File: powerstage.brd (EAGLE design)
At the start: 41.9 x 43.5 mm, 44 parts, among them CON1 PINHEAD_1X10-2-FEMALE, CON2 PINHEAD_1X10-2-FEMALE, CON3 BATTERY_CON-2P-XT30-RA, IC1 MCP9700, Q1 BUK9K6R2-40E,115, Q2 BUK9K6R2-40E,115, Q3 BUK9K6R2-40E,115

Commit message: Bloody fiducial marks
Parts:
- moved U$9 38.6 mm to (11.3, 16.6), flipped to the bottom
- moved U$8 9.24 mm to (-16.6, -11.3), flipped to the bottom
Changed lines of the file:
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@@
 <setting verticaltext="up"/>
 </settings>
-<grid distance="0.25" unitdist="mm" unit="mm" style="lines" multiple="1" display="yes" altdistance="5" altunitdist="mil" altunit="mil"/>
+<grid distance="0.1" unitdist="mm" unit="mm" style="lines" multiple="1" display="yes" altdistance="5" altunitdist="mil" altunit="mil"/>
 <layers>
 <layer number="1" name="Top" color="4" fill="1" visible="no" active="yes"/>
@@
 <layer number="200" name="200bmp" color="1" fill="10" visible="no" active="yes"/>
 <layer number="201" name="201bmp" color="2" fill="10" visible="no" active="yes"/>
-<layer number="202" name="202bmp" color="3" fill="10" visible="yes" active="yes"/>
+<layer number="202" name="202bmp" color="3" fill="10" visible="no" active="yes"/>
 <layer number="203" name="203bmp" color="4" fill="10" visible="no" active="yes"/>
 <layer number="204" name="204bmp" color="5" fill="10" visible="no" active="yes"/>
@@
 </layers>
 <board>
-<fusionsync huburn="a.cGVyc29uYWw6dWUyYWE4ZDY4" projecturn="a.cGVyc29uYWw6dWUyYWE4ZDY4IzIwMTkwMzI5MTg1MjAzMjgx" f3durn="urn:adsk.wipprod:dm.lineage:ZAJHTluVSR69FIREnNfqcQ" pcbguid="7c6f9a56-3587-45a7-8229-92f35c80dc4b" lastpulledtime="" lastsyncedchangeguid="23cae763-0e7c-6782-396c-fa785399b2ba"/>
+<fusionsync huburn="a.cGVyc29uYWw6dWUyYWE4ZDY4" projecturn="a.cGVyc29uYWw6dWUyYWE4ZDY4IzIwMTkwMzI5MTg1MjAzMjgx" f3durn="urn:adsk.wipprod:dm.lineage:ZAJHTluVSR69FIREnNfqcQ" pcbguid="7c6f9a56-3587-45a7-8229-92f35c80dc4b" lastpulledtime="" lastsyncedchangeguid="72de28a5-7bf0-bc42-2327-0a8f38e2b9e8"/>
 <plain>
 <wire x1="0" y1="0" x2="0" y2="21" width="0.1524" layer="49" style="shortdash" locked="yes"/>
@@
 <element name="U$2" library="logo" library_urn="urn:adsk.eagle:library:6668987" package="DUCK-8.5X7.5-MASK" value="" x="-4.5" y="-22.475" smashed="yes"/>
 <element name="U$4" library="logo" library_urn="urn:adsk.eagle:library:6668987" package="OSHW-10.5X11.5" value="" x="-1.525" y="-5.525" smashed="yes" rot="MR0"/>
-<element name="U$8" library="usb2can_master_lib" package="FIDUCIA-MOUNT" value="FIDUCIALMOUNT" x="-13.5" y="-20" populate="no" smashed="yes"/>
-<element name="U$9" library="usb2can_master_lib" package="FIDUCIA-MOUNT" value="FIDUCIALMOUNT" x="12.5" y="-22" populate="no" smashed="yes"/>
+<element name="U$8" library="usb2can_master_lib" package="FIDUCIA-MOUNT" value="FIDUCIALMOUNT" x="-16.6" y="-11.3" populate="no" smashed="yes" rot="MR0"/>
+<element name="U$9" library="usb2can_master_lib" package="FIDUCIA-MOUNT" value="FIDUCIALMOUNT" x="11.3" y="16.6" populate="no" smashed="yes" rot="MR0"/>
 <element name="U$10" library="usb2can_master_lib" package="FIDUCIA-MOUNT" value="FIDUCIALMOUNT" x="11.3" y="16.6" populate="no" smashed="yes"/>
 <element name="U$12" library="usb2can_master_lib" package="FIDUCIA-MOUNT" value="FIDUCIALMOUNT" x="-16.6" y="-11.3" populate="no" smashed="yes"/>
@@
 <wire x1="16.35" y1="-0.15" x2="17.2" y2="-1" width="0.25" layer="1"/>
 <wire x1="11.65" y1="-0.15" x2="16.35" y2="-0.15" width="0.25" layer="1"/>
-<wire x1="6.05" y1="4" x2="6.775" y2="5.875" width="0" layer="19" extent="1-1"/>
+<wire x1="6.775" y1="5.875" x2="6.05" y2="4" width="0" layer="19" extent="1-1"/>
 </signal>
 <signal name="PHASE_A" class="1">

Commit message: damn duck logo
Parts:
- U$2: device logo:DUCK-8.5X7.5-MASK -> logo:DUCK_6X5
- moved U$2 2.89 mm to (-3.00, -20.0)
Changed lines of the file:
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@@
 <setting verticaltext="up"/>
 </settings>
-<grid distance="0.1" unitdist="mm" unit="mm" style="lines" multiple="1" display="yes" altdistance="5" altunitdist="mil" altunit="mil"/>
+<grid distance="0.5" unitdist="mm" unit="mm" style="lines" multiple="1" display="yes" altdistance="5" altunitdist="mil" altunit="mil"/>
 <layers>
-<layer number="1" name="Top" color="4" fill="1" visible="no" active="yes"/>
+<layer number="1" name="Top" color="4" fill="1" visible="yes" active="yes"/>
 <layer number="2" name="Route2" color="43" fill="3" visible="no" active="yes"/>
 <layer number="3" name="Route3" color="17" fill="1" visible="no" active="no"/>
@@
 <layer number="14" name="Route14" color="22" fill="1" visible="no" active="no"/>
 <layer number="15" name="Route15" color="46" fill="6" visible="no" active="yes"/>
-<layer number="16" name="Bottom" color="1" fill="1" visible="yes" active="yes"/>
+<layer number="16" name="Bottom" color="1" fill="1" visible="no" active="yes"/>
 <layer number="17" name="Pads" color="2" fill="1" visible="yes" active="yes"/>
 <layer number="18" name="Vias" color="2" fill="1" visible="yes" active="yes"/>
 <layer number="19" name="Unrouted" color="6" fill="1" visible="no" active="yes"/>
 <layer number="20" name="Dimension" color="24" fill="1" visible="yes" active="yes"/>
-<layer number="21" name="tPlace" color="7" fill="1" visible="no" active="yes"/>
-<layer number="22" name="bPlace" color="7" fill="1" visible="yes" active="yes"/>
-<layer number="23" name="tOrigins" color="15" fill="1" visible="no" active="yes"/>
-<layer number="24" name="bOrigins" color="15" fill="1" visible="yes" active="yes"/>
-<layer number="25" name="tNames" color="7" fill="1" visible="no" active="yes"/>
-<layer number="26" name="bNames" color="7" fill="1" visible="yes" active="yes"/>
+<layer number="21" name="tPlace" color="7" fill="1" visible="yes" active="yes"/>
+<layer number="22" name="bPlace" color="7" fill="1" visible="no" active="yes"/>
+<layer number="23" name="tOrigins" color="15" fill="1" visible="yes" active="yes"/>
+<layer number="24" name="bOrigins" color="15" fill="1" visible="no" active="yes"/>
+<layer number="25" name="tNames" color="7" fill="1" visible="yes" active="yes"/>
+<layer number="26" name="bNames" color="7" fill="1" visible="no" active="yes"/>
 <layer number="27" name="tValues" color="7" fill="1" visible="no" active="yes"/>
 <layer number="28" name="bValues" color="7" fill="1" visible="no" active="yes"/>
@@
 <layer number="49" name="Reference" color="7" fill="1" visible="no" active="yes"/>
 <layer number="50" name="dxf" color="7" fill="1" visible="no" active="yes"/>
-<layer number="51" name="tDocu" color="7" fill="1" visible="no" active="yes"/>
-<layer number="52" name="bDocu" color="7" fill="1" visible="yes" active="yes"/>
+<layer number="51" name="tDocu" color="7" fill="1" visible="yes" active="yes"/>
+<layer number="52" name="bDocu" color="7" fill="1" visible="no" active="yes"/>
 <layer number="53" name="tGND_GNDA" color="7" fill="9" visible="no" active="no"/>
 <layer number="54" name="bGND_GNDA" color="1" fill="9" visible="no" active="no"/>
@@
 </layers>
 <board>
-<fusionsync huburn="a.cGVyc29uYWw6dWUyYWE4ZDY4" projecturn="a.cGVyc29uYWw6dWUyYWE4ZDY4IzIwMTkwMzI5MTg1MjAzMjgx" f3durn="urn:adsk.wipprod:dm.lineage:ZAJHTluVSR69FIREnNfqcQ" pcbguid="7c6f9a56-3587-45a7-8229-92f35c80dc4b" lastpulledtime="" lastsyncedchangeguid="72de28a5-7bf0-bc42-2327-0a8f38e2b9e8"/>
+<fusionsync huburn="a.cGVyc29uYWw6dWUyYWE4ZDY4" projecturn="a.cGVyc29uYWw6dWUyYWE4ZDY4IzIwMTkwMzI5MTg1MjAzMjgx" f3durn="urn:adsk.wipprod:dm.lineage:ZAJHTluVSR69FIREnNfqcQ" pcbguid="7c6f9a56-3587-45a7-8229-92f35c80dc4b" lastpulledtime="" lastsyncedchangeguid="29ea1aaf-b1cc-dbc7-7fdc-4014fc0b66bb"/>
 <plain>
 <wire x1="0" y1="0" x2="0" y2="21" width="0.1524" layer="49" style="shortdash" locked="yes"/>
@@
 </attributes>
 <variantdefs>
-<variantdef name="BASIC" current="yes"/>
+<variantdef name="BASIC"/>
 </variantdefs>
 <classes>
@@
 </autorouter>
 <elements>
-<element name="A" library="PADS" library_urn="urn:adsk.eagle:library:3188696" package="HOLE_2" package3d_urn="urn:adsk.eagle:package:4854323/1" value="PAD-HOLE_2" x="5" y="18" locked="yes" populate="no" smashed="yes">
+<element name="A" library="PADS" library_urn="urn:adsk.eagle:library:3188696" package="HOLE_2" package3d_urn="urn:adsk.eagle:package:4854323/1" value="PAD-HOLE_2" x="5" y="18" locked="yes" smashed="yes">
 <attribute name="BOM" value="EXCLUDE" x="5" y="18" size="1.778" layer="27" display="off"/>
 <attribute name="NAME" x="5" y="20" size="1" layer="25" font="vector" ratio="15" align="center"/>
@@
 <attribute name="VALUE" x="14.7" y="1.75" size="0.5" layer="27" font="vector" ratio="15" rot="R180" align="center"/>
 </element>
-<element name="B" library="PADS" library_urn="urn:adsk.eagle:library:3188696" package="HOLE_2" package3d_urn="urn:adsk.eagle:package:4854323/1" value="PAD-HOLE_2" x="-5" y="18" locked="yes" populate="no" smashed="yes">
+<element name="B" library="PADS" library_urn="urn:adsk.eagle:library:3188696" package="HOLE_2" package3d_urn="urn:adsk.eagle:package:4854323/1" value="PAD-HOLE_2" x="-5" y="18" locked="yes" smashed="yes">
 <attribute name="BOM" value="EXCLUDE" x="-5" y="18" size="1.778" layer="27" display="off"/>
 <attribute name="NAME" x="-5" y="20" size="1" layer="25" font="vector" ratio="15" align="center"/>
@@
 <attribute name="VALUE" x="-14.7" y="-2.05" size="0.5" layer="27" font="vector" ratio="15" align="center"/>
 </element>
-<element name="C" library="PADS" library_urn="urn:adsk.eagle:library:3188696" package="HOLE_2" package3d_urn="urn:adsk.eagle:package:4854323/1" value="PAD-HOLE_2" x="0" y="18" locked="yes" populate="no" smashed="yes">
+<element name="C" library="PADS" library_urn="urn:adsk.eagle:library:3188696" package="HOLE_2" package3d_urn="urn:adsk.eagle:package:4854323/1" value="PAD-HOLE_2" x="0" y="18" locked="yes" smashed="yes">
 <attribute name="BOM" value="EXCLUDE" x="0" y="18" size="1.778" layer="27" display="off"/>
 <attribute name="NAME" x="0" y="20" size="1" layer="25" font="vector" ratio="15" align="center"/>
@@
 <attribute name="VALUE" x="14.55" y="-5" size="0.5" layer="27" font="vector" ratio="15" rot="R180" align="center"/>
 </element>
-<element name="S1" library="misc" library_urn="urn:adsk.eagle:library:5347860" package="SENSE-0.6" value="SENSE" x="0.75" y="5.625" populate="no" smashed="yes" rot="R90">
+<element name="S1" library="misc" library_urn="urn:adsk.eagle:library:5347860" package="SENSE-0.6" value="SENSE" x="0.75" y="5.625" smashed="yes" rot="R90">
 <attribute name="BOM" value="EXCLUDE" x="63.75" y="-20.375" size="1.778" layer="27" rot="R90" display="off"/>
 </element>
@@
 <element name="U$13" library="pixhawk_esc_1.5_master_lib" package="ZUBAX_LOGO_5X10" value="" x="-6.225" y="-5.475" smashed="yes"/>
 <element name="U$1" library="pixhawk_esc_1.5_master_lib" package="ZUBAX_LOGO_5X10" value="" x="12.7" y="-3.5" smashed="yes" rot="MR0"/>
-<element name="U$2" library="logo" library_urn="urn:adsk.eagle:library:6668987" package="DUCK-8.5X7.5-MASK" value="" x="-4.5" y="-22.475" smashed="yes"/>
 <element name="U$4" library="logo" library_urn="urn:adsk.eagle:library:6668987" package="OSHW-10.5X11.5" value="" x="-1.525" y="-5.525" smashed="yes" rot="MR0"/>
-<element name="U$8" library="usb2can_master_lib" package="FIDUCIA-MOUNT" value="FIDUCIALMOUNT" x="-16.6" y="-11.3" populate="no" smashed="yes" rot="MR0"/>
-<element name="U$9" library="usb2can_master_lib" package="FIDUCIA-MOUNT" value="FIDUCIALMOUNT" x="11.3" y="16.6" populate="no" smashed="yes" rot="MR0"/>
-<element name="U$10" library="usb2can_master_lib" package="FIDUCIA-MOUNT" value="FIDUCIALMOUNT" x="11.3" y="16.6" populate="no" smashed="yes"/>
-<element name="U$12" library="usb2can_master_lib" package="FIDUCIA-MOUNT" value="FIDUCIALMOUNT" x="-16.6" y="-11.3" populate="no" smashed="yes"/>
+<element name="U$8" library="usb2can_master_lib" package="FIDUCIA-MOUNT" value="FIDUCIALMOUNT" x="-16.6" y="-11.3" smashed="yes" rot="MR0"/>
+<element name="U$9" library="usb2can_master_lib" package="FIDUCIA-MOUNT" value="FIDUCIALMOUNT" x="11.3" y="16.6" smashed="yes" rot="MR0"/>
+<element name="U$10" library="usb2can_master_lib" package="FIDUCIA-MOUNT" value="FIDUCIALMOUNT" x="11.3" y="16.6" smashed="yes"/>
+<element name="U$12" library="usb2can_master_lib" package="FIDUCIA-MOUNT" value="FIDUCIALMOUNT" x="-16.6" y="-11.3" smashed="yes"/>
+<element name="U$2" library="logo" library_urn="urn:adsk.eagle:library:6668987" package="DUCK_6X5" value="" x="-3" y="-20" smashed="yes"/>
 </elements>
 <signals>

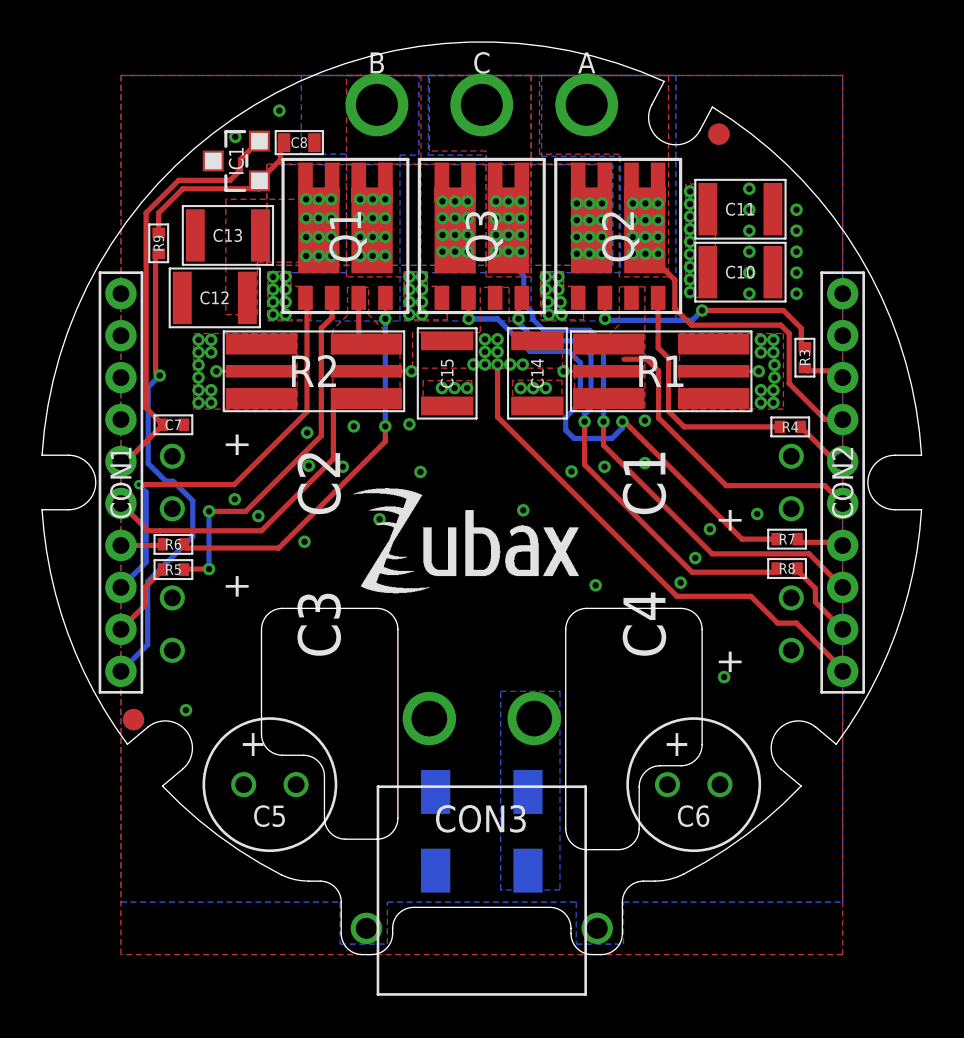
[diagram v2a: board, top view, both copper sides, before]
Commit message: TVS diode replaced
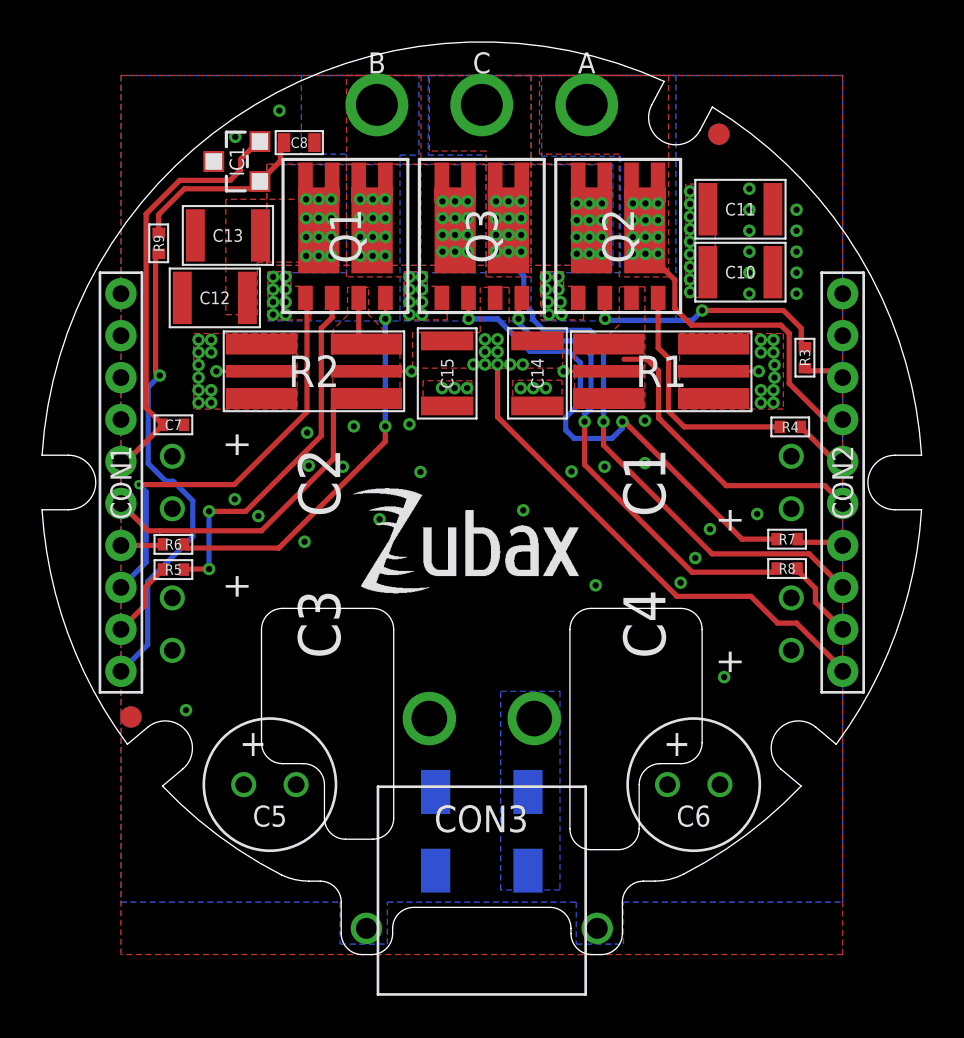
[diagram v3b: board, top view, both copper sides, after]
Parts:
- D1, D2: value PTVS36VP1UP,115-36V-SOD128 -> PTVS33VP1UTP,115-36V-SOD128
- moved U$12 0.18 mm to (-16.7, -11.2)
- moved U$8 0.18 mm to (-16.7, -11.2)
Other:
- outline, holes or cut-outs redrawn
